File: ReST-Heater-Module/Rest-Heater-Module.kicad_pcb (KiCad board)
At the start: 2 copper layers, 24.5 x 29.5 mm, 35 parts

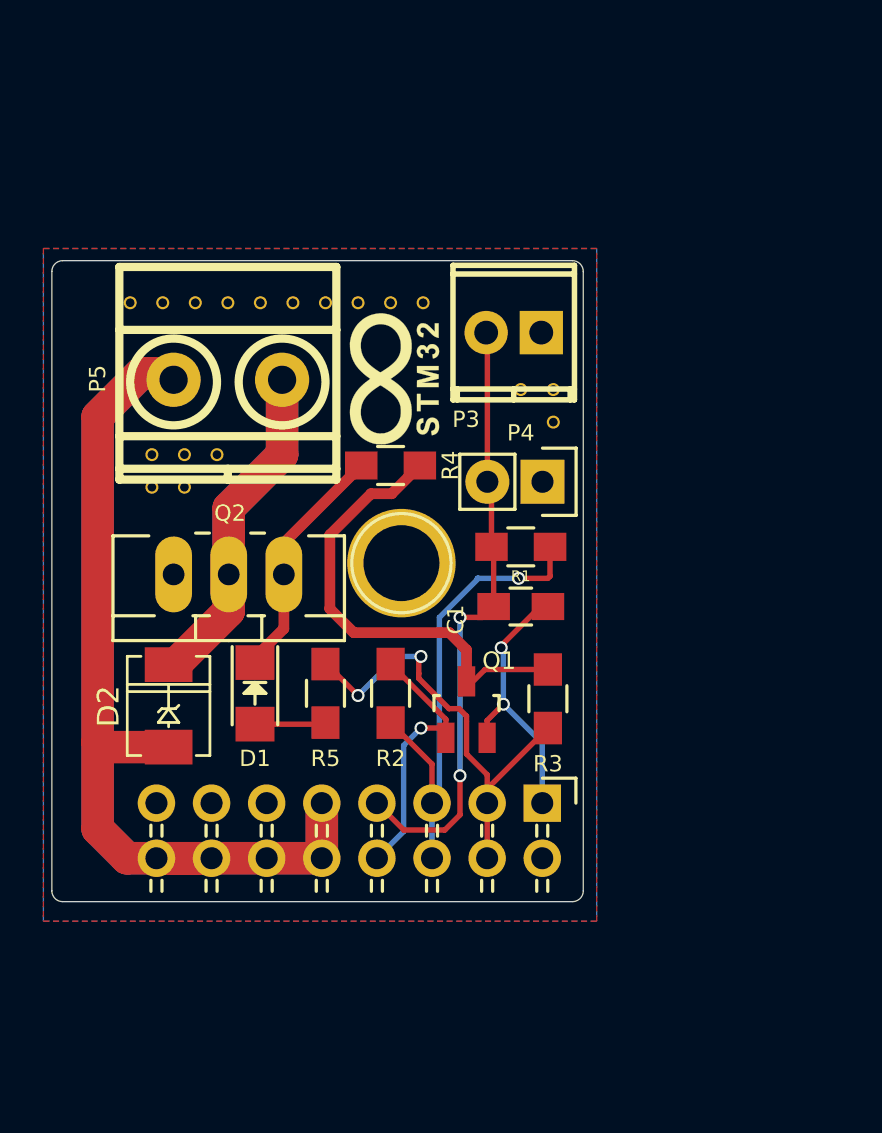
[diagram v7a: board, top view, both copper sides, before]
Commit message: Reworked Modules to sit ontop of the mainboard
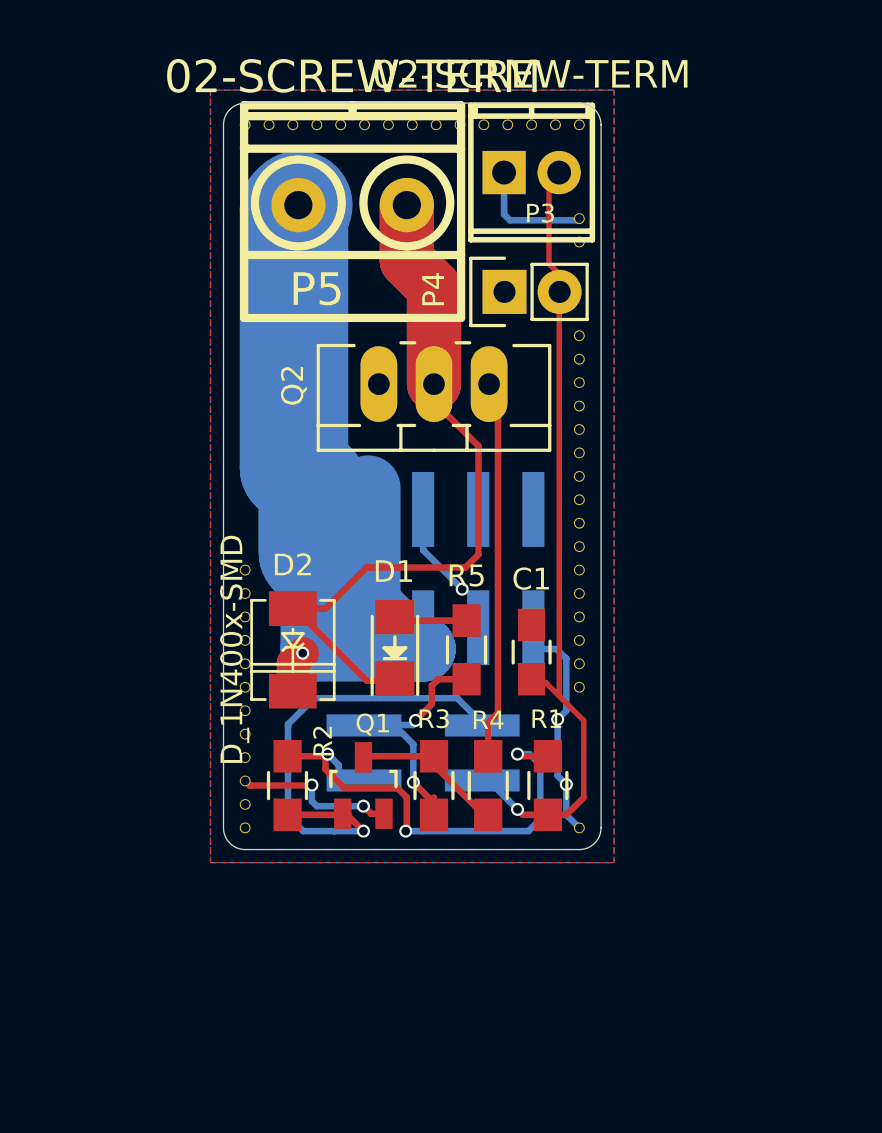
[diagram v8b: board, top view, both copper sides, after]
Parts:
- removed the ? at (156.0, 112.5)
- removed the ? at (148.5, 107.0)
- removed the ? at (147.0, 107.0)
- removed the ? at (145.5, 107.0)
- removed the ? at (144.0, 107.0)
- removed the ? at (142.5, 107.0)
- removed the ? at (141.0, 107.0)
- removed the ? at (139.5, 107.0)
- removed the ? at (138.0, 107.0)
- removed the ? at (148.4, 112.7)
- removed the ? at (148.8, 110.5)
- removed the ? at (156.0, 111.0)
- removed the ? at (149.0, 119.0)
- removed the ? at (136.5, 107.0)
- removed the ? at (154.5, 111.0)
- removed the ? at (139.0, 115.5)
- removed the ? at (137.5, 115.5)
- removed the ? at (140.5, 114.0)
- removed the ? at (139.0, 114.0)
- removed the ? at (137.5, 114.0)
- removed the ? at (150.0, 107.0)
- added ?: , ReST-Library:1pin, F.Cu at (157.2, 124.7)
- added ?: , ReST-Library:1pin, F.Cu at (157.2, 116.1)
- added ?: , ReST-Library:1pin, F.Cu at (157.2, 115.0)
- added ?: , ReST-Library:1pin, F.Cu at (157.2, 113.9)
- added ?: , ReST-Library:1pin, F.Cu at (157.2, 112.8)
- added ?: , ReST-Library:1pin, F.Cu at (157.2, 111.8)
- added ?: , ReST-Library:1pin, F.Cu at (157.2, 110.7)
- added ?: , ReST-Library:1pin, F.Cu at (157.2, 109.6)
- added ?: , ReST-Library:1pin, F.Cu at (157.2, 108.5)
- added ?: , ReST-Library:1pin, F.Cu at (157.2, 104.2)
- added ?: , ReST-Library:1pin, F.Cu at (157.2, 103.1)
- added ?: , ReST-Library:1pin, F.Cu at (157.2, 131.2)
- added ?: , ReST-Library:1pin, F.Cu at (141.8, 131.2)
- added ?: , ReST-Library:1pin, F.Cu at (141.8, 130.1)
- added ?: , ReST-Library:1pin, F.Cu at (141.8, 129.0)
- added ?: , ReST-Library:1pin, F.Cu at (141.8, 128.0)
- added ?: , ReST-Library:1pin, F.Cu at (141.8, 126.9)
- added ?: , ReST-Library:1pin, F.Cu at (141.8, 125.8)
- added ?: , ReST-Library:1pin, F.Cu at (141.8, 124.7)
- added ?: , ReST-Library:1pin, F.Cu at (141.8, 123.6)
- added ?: , ReST-Library:1pin, F.Cu at (141.8, 122.6)
- added ?: , ReST-Library:1pin, F.Cu at (141.8, 121.5)
- added ?: , ReST-Library:1pin, F.Cu at (157.2, 123.6)
- added ?: , ReST-Library:1pin, F.Cu at (141.8, 120.4)
- added ?: , ReST-Library:1pin, F.Cu at (141.8, 119.3)
- added ?: , ReST-Library:1pin, F.Cu at (141.8, 99.9)
- added ?: , ReST-Library:1pin, F.Cu at (157.2, 98.8)
- added ?: , ReST-Library:1pin, F.Cu at (156.1, 98.8)
- added ?: , ReST-Library:1pin, F.Cu at (155.0, 98.8)
- added ?: , ReST-Library:1pin, F.Cu at (153.9, 98.8)
- added ?: , ReST-Library:1pin, F.Cu at (152.8, 98.8)
- added ?: , ReST-Library:1pin, F.Cu at (151.7, 98.8)
- added ?: , ReST-Library:1pin, F.Cu at (150.6, 98.8)
- added ?: , ReST-Library:1pin, F.Cu at (157.2, 122.6)
- added ?: , ReST-Library:1pin, F.Cu at (149.5, 98.8)
- added ?: , ReST-Library:1pin, F.Cu at (148.4, 98.8)
- added ?: , ReST-Library:1pin, F.Cu at (147.3, 98.8)
- added ?: , ReST-Library:1pin, F.Cu at (146.2, 98.8)
- added ?: , ReST-Library:1pin, F.Cu at (145.1, 98.8)
- added ?: , ReST-Library:1pin, F.Cu at (144.0, 98.8)
- added ?: , ReST-Library:1pin, F.Cu at (142.9, 98.8)
- added ?: , ReST-Library:1pin, F.Cu at (141.8, 98.8)
- added ?: , ReST-Library:1pin, F.Cu at (157.2, 121.5)
- added ?: , ReST-Library:1pin, F.Cu at (157.2, 120.4)
- added ?: , ReST-Library:1pin, F.Cu at (157.2, 119.3)
- added ?: , ReST-Library:1pin, F.Cu at (157.2, 118.2)
- added ?: , ReST-Library:1pin, F.Cu at (157.2, 117.2)
- added P2: CONN_02X05, ReST-Library:bb02-hp10, B.Cu at (150.0, 119.2)
- C1: value (none) -> 10uF
- D1: value (none) -> LED
- D2: value (none) -> D_1N400x-SMD; footprint ReST-Library:DO-214AC(SMA) -> ReST-Library:DO-214AC.SMA
- P1: value (none) -> CONN_02X02; footprint ReST-Library:Pin_Header_Angled_2x08 -> ReST-Library:bb02-hp04; moved to B.Cu
- P3: value (none) -> 02-SCREW-TERM; footprint ReST-Library:screw-2,54-2P -> ReST-Library:screw-2.54-2P
- P4: value (none) -> 01X02-MALE
- P5: value (none) -> 02-SCREW-TERM
- Q1: value (none) -> Q_BSH105
- Q2: value (none) -> Q_AOT240L
- R1: value (none) -> 4.7K
- R2, R3: value (none) -> 100K
- R4: value (none) -> 22R
- R5: value (none) -> 1K
- moved R4 15.4 mm to (153.0, 129.2), turned to 90 degrees
- moved Q2 12.9 mm to (150.5, 110.8)
- moved R1 11.1 mm to (155.8, 129.2), turned to 90 degrees
- moved P5 9.89 mm to (146.8, 102.5), turned to 180 degrees
- moved P4 8.92 mm to (153.8, 106.5), turned to 90 degrees
- moved P3 7.42 mm to (155.0, 101.0), turned to 180 degrees
- moved R5 6.80 mm to (152.0, 123.0), turned to 270 degrees
- moved D1 6.78 mm to (148.7, 122.9), turned to 90 degrees
- moved R3 6.60 mm to (150.5, 129.2)
- moved R2 6.37 mm to (143.8, 129.2), turned to 90 degrees
- moved D2 6.28 mm to (144.0, 123.0), turned to 270 degrees
- moved P1 5.96 mm to (150.0, 127.8), turned to 90 degrees
- moved Q1 5.90 mm to (147.2, 129.2)
- moved C1 2.16 mm to (155.0, 123.1), turned to 90 degrees
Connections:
- D2 pad 2: Net-(D2-Pad2) -> Net-(D1-Pad1)
- P1 pad 1: GND -> +3V3
- P1 pad 2: GND -> /T1
- P1 pad 4: +5V -> /PWM-HEATER
- P5 pad 1: +12V -> Net-(D1-Pad1)
- P5 pad 2: Net-(D2-Pad2) -> +12V
- Q2 pad 1: Net-(D1-Pad1) -> Net-(Q2-Pad1)
- Q2 pad 2: Net-(D2-Pad2) -> Net-(D1-Pad1)
- R4 pad 2: Net-(D1-Pad1) -> Net-(Q2-Pad1)
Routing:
- net Net-(D1-Pad1): track 12.3 -> 41.9 mm
- net +12V: track 79.4 -> 49.9 mm, vias 0 -> 1
- net Net-(D2-Pad2): track 26.1 -> 0.00 mm
- net Net-(Q2-Pad1): track 0.00 -> 17.5 mm
- net GND: track 12.5 -> 28.5 mm, vias 2 -> 5
- net Net-(Q1-Pad3): track 21.8 -> 7.12 mm
- net /PWM-HEATER: track 12.2 -> 24.0 mm
- net /T1: track 28.4 -> 36.9 mm, vias 2 -> 1
- net +5V: track 21.3 -> 15.1 mm
- net +3V3: track 23.1 -> 21.7 mm, vias 1 -> 3
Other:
- board size 24.5 x 29.5 mm -> 17.4 x 34.4 mm
- board text removed: "ReST32 Heater Rev. A | Test @maker_berry"
